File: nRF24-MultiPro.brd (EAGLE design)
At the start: 26 x 38.1 mm, 13 parts, among them IC1 SPX3819, J1 22-27-2051-05, Q1 BSS123

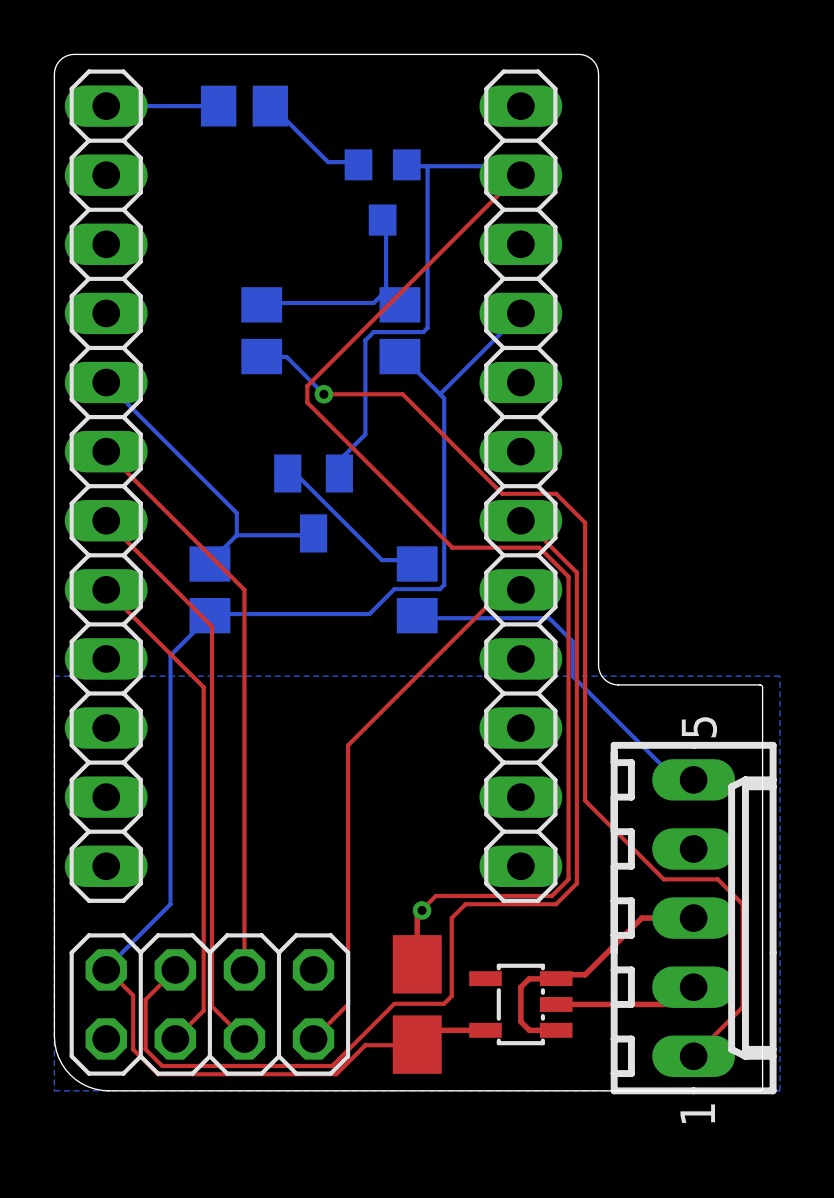
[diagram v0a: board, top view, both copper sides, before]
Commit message: v1.1 pcb
- 470pF for low noise
- slightly rearanged SMDs
- manualy traced some wires
- GND and VCC upped to 8mil
- added logo
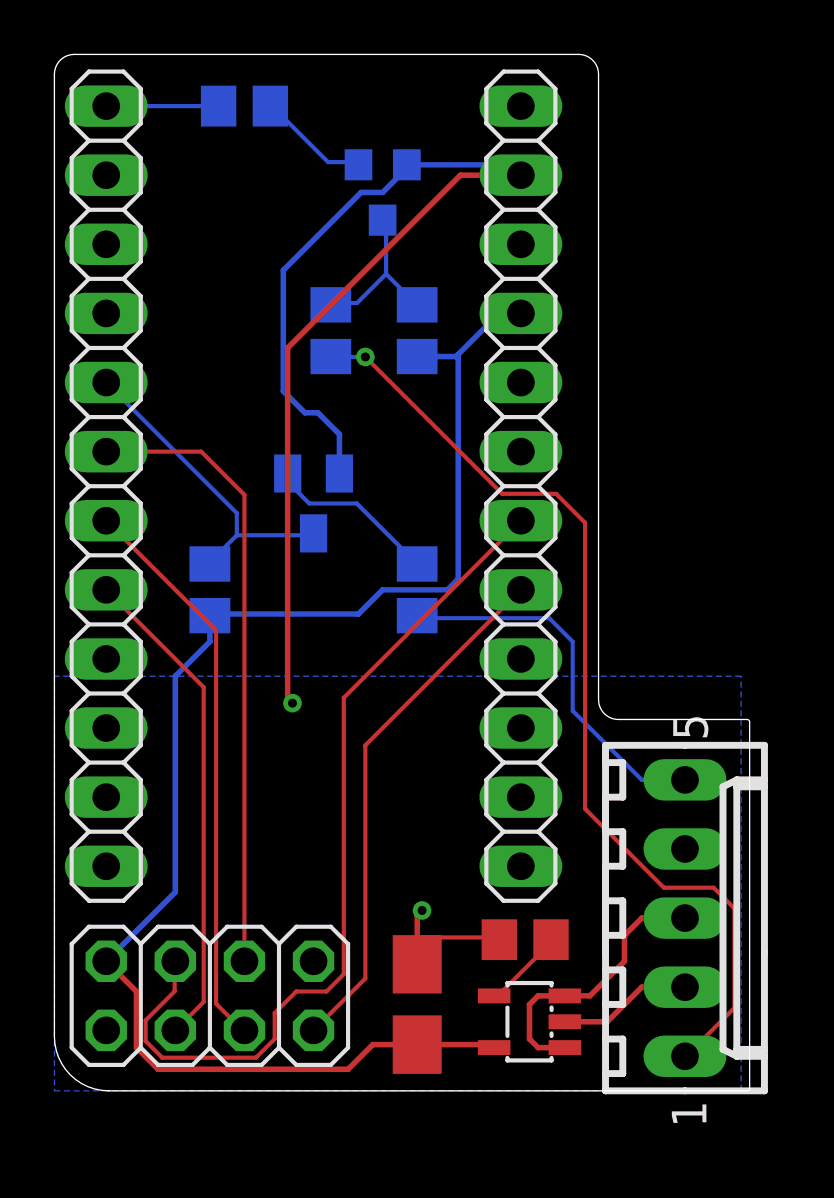
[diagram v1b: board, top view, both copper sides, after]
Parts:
- added C2: 470pF, resistor:C0805
- C1: value (none) -> 2.2uF
- moved R4 2.54 mm to (10.2, 27.9)
- moved IC1 0.71 mm to (17.5, 2.54)
- moved R5 0.64 mm to (13.3, 27.9)
- moved J1 0.32 mm to (23.2, 6.35)
- moved JP1 0.32 mm to (5.71, 3.49)
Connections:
- new net N$14: C2.1, IC1.4
- net GND: now also C2.2
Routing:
- net GND: track 66.5 -> 54.6 mm, vias 1 -> 2
- net N$3: track 38.2 -> 32.1 mm
- net N$14: track 0.00 -> 3.02 mm
- net N$12: track 9.00 -> 6.22 mm
- net N$13: track 38.3 -> 35.6 mm
- net N$5: track 21.2 -> 22.9 mm
- net N$11: track 20.0 -> 19.3 mm
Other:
- board size 26 x 38.1 mm -> 25.6 x 38.1 mm
- board text added: "nRF24 MultiPro mozgy - v1.1"
- board text removed: "mozgy - ver1.0"
- board text removed: "nrf24 Multipro"
